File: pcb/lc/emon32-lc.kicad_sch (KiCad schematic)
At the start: 49 parts, among them J3 Conn_02x05_Odd_Even, J4 RJ12, J5 Conn_Coaxial, J6 USB_C_Receptacle_USB2.0, J7 Conn_01x03_Male, J8 Conn_02x04_Odd_Even, J9 Conn_01x03_Male, SW1 SW_Push, U2 AT24CS01-STUM, U3 ATSAMD11D14A-M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

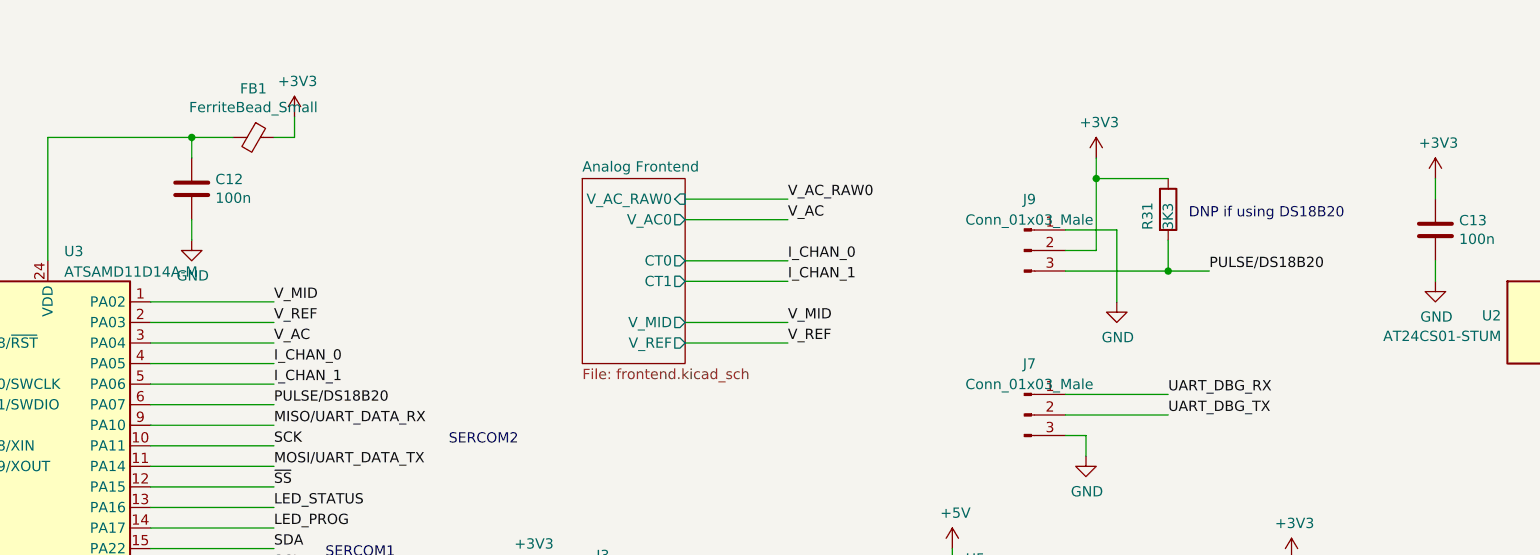
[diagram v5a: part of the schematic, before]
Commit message: * [LC]
  - Move ESP header out of RFM footprint to remove short risk
  - Remove all vias inside RFM footprint
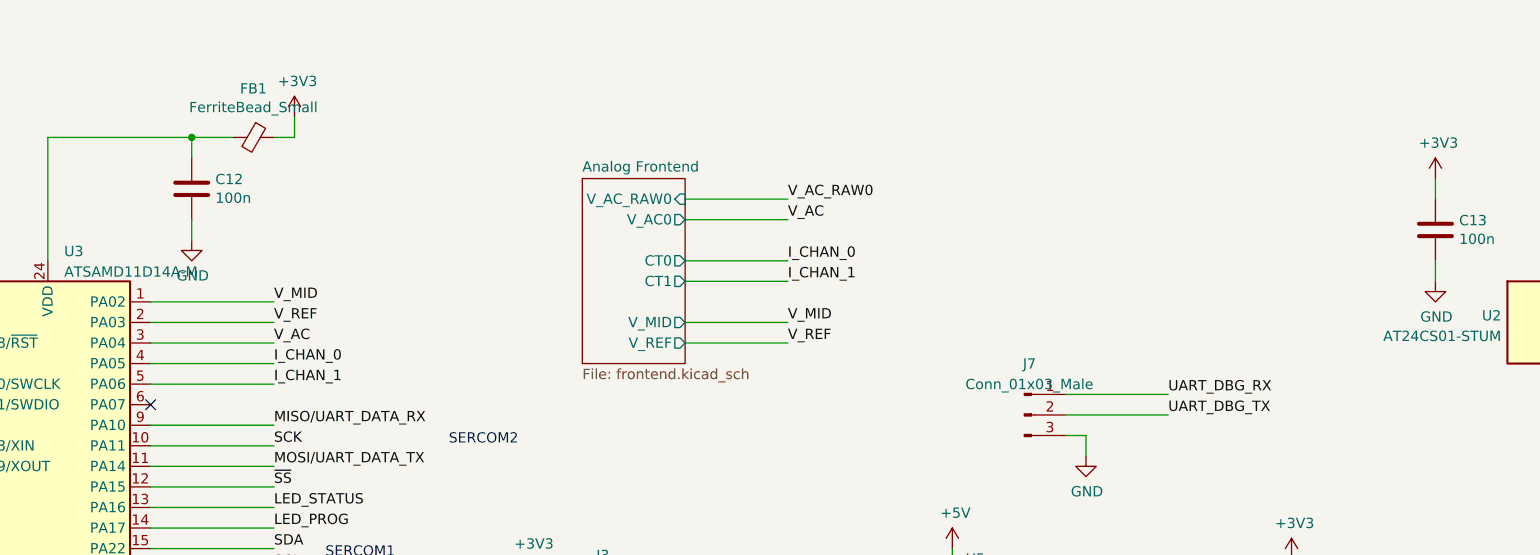
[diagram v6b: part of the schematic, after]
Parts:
- removed J9: Conn_01x03_Male, Connector_PinHeader_2.54mm:PinHeader_1x03_P2.54mm_Vertical, symbol Connector:Conn_01x03_Male
- removed R31: 3K3, Resistor_SMD:R_0402_1005Metric, symbol Device:R
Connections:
- net PULSE/DS18B20: no longer names the net of U3.6 (PA07)
- no-connect marks 18 -> 19
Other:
- note removed: "DNP if using DS18B20"
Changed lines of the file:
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@@
   (junction (at 27.94 24.13) (diameter 0) (color 0 0 0 0)
   )
-  (junction (at 177.8 25.4) (diameter 0) (color 0 0 0 0)
-  )
   (junction (at 124.46 129.54) (diameter 0) (color 0 0 0 0)
   )
   (junction (at 107.95 82.55) (diameter 0) (color 0 0 0 0)
-  )
-  (junction (at 186.69 36.83) (diameter 0) (color 0 0 0 0)
   )
   (junction (at 66.04 20.32) (diameter 0) (color 0 0 0 0)
@@
   (no_connect (at 60.96 81.28))
   (no_connect (at 50.8 157.48))
+  (no_connect (at 60.96 53.34))
   (no_connect (at 248.92 102.87))
   (wire (pts (xy 80.01 171.45) (xy 80.01 185.42))
@@
     (stroke (width 0) (type default))
   )
-  (wire (pts (xy 177.8 25.4) (xy 186.69 25.4))
-    (stroke (width 0) (type default))
-  )
   (wire (pts (xy 219.71 144.78) (xy 228.6 144.78))
     (stroke (width 0) (type default))
@@
     (stroke (width 0) (type default))
   )
-  (wire (pts (xy 177.8 25.4) (xy 177.8 22.86))
-    (stroke (width 0) (type default))
-  )
   (wire (pts (xy 96.52 129.54) (xy 100.33 129.54))
     (stroke (width 0) (type default))
@@
     (stroke (width 0) (type default))
   )
-  (wire (pts (xy 180.34 31.75) (xy 180.34 40.64))
-    (stroke (width 0) (type default))
-  )
   (wire (pts (xy 118.11 129.54) (xy 120.65 129.54))
     (stroke (width 0) (type default))
@@
     (stroke (width 0) (type default))
   )
-  (wire (pts (xy 186.69 33.02) (xy 186.69 36.83))
-    (stroke (width 0) (type default))
-  )
   (wire (pts (xy 60.96 43.18) (xy 76.2 43.18))
     (stroke (width 0) (type default))
@@
     (stroke (width 0) (type default))
   )
-  (wire (pts (xy 60.96 53.34) (xy 76.2 53.34))
-    (stroke (width 0) (type default))
-  )
   (wire (pts (xy 60.96 48.26) (xy 76.2 48.26))
     (stroke (width 0) (type default))
@@
     (stroke (width 0) (type default))
   )
-  (wire (pts (xy 173.99 34.29) (xy 177.8 34.29))
-    (stroke (width 0) (type default))
-  )
   (wire (pts (xy 241.3 142.24) (xy 247.65 142.24))
     (stroke (width 0) (type default))
@@
     (stroke (width 0) (type default))
   )
-  (wire (pts (xy 173.99 36.83) (xy 186.69 36.83))
-    (stroke (width 0) (type default))
-  )
   (wire (pts (xy 25.4 88.9) (xy 22.86 88.9))
     (stroke (width 0) (type default))
@@
     (stroke (width 0) (type default))
   )
-  (wire (pts (xy 177.8 25.4) (xy 177.8 34.29))
-    (stroke (width 0) (type default))
-  )
   (wire (pts (xy 50.8 129.54) (xy 69.85 129.54))
     (stroke (width 0) (type default))
@@
     (stroke (width 0) (type default))
   )
-  (wire (pts (xy 173.99 31.75) (xy 180.34 31.75))
-    (stroke (width 0) (type default))
-  )
   (wire (pts (xy 176.53 57.15) (xy 176.53 59.69))
     (stroke (width 0) (type default))
@@
     (stroke (width 0) (type default))
   )
-  (wire (pts (xy 186.69 36.83) (xy 191.77 36.83))
-    (stroke (width 0) (type default))
-  )
   (wire (pts (xy 27.94 50.8) (xy 25.4 50.8))
     (stroke (width 0) (type default))
@@
   (wire (pts (xy 139.7 152.4) (xy 139.7 149.86))
     (stroke (width 0) (type default))
-  )
-  (text "DNP if using DS18B20" (at 189.23 30.48 0)
-    (effects (font (size 1.27 1.27)) (justify left bottom))
   )
   (text "emon32 Low Cost" (at 177.8 171.45 0)
@@
     (effects (font (size 1.27 1.27)) (justify left bottom))
   )
-  (label "PULSE{slash}DS18B20" (at 191.77 36.83 0) (fields_autoplaced)
-    (effects (font (size 1.27 1.27)) (justify left bottom))
-  )
   (label "MOSI{slash}UART_DATA_TX" (at 219.71 144.78 180) (fields_autoplaced)
     (effects (font (size 1.27 1.27)) (justify right bottom))
@@
   )
   (label "V_AC" (at 76.2 45.72 0) (fields_autoplaced)
-    (effects (font (size 1.27 1.27)) (justify left bottom))
-  )
-  (label "PULSE{slash}DS18B20" (at 76.2 53.34 0) (fields_autoplaced)
     (effects (font (size 1.27 1.27)) (justify left bottom))
   )
@@
     )
   )
-  (symbol (lib_id "power:+3V3") (at 177.8 22.86 0) (unit 1)
-    (in_bom yes) (on_board yes) (dnp no)
-    (property "Reference" "#PWR0133" (at 177.8 26.67 0)
-      (effects (font (size 1.27 1.27)) hide)
-    )
-    (property "Value" "+3V3" (at 178.181 18.4658 0)
-      (effects (font (size 1.27 1.27)))
-    )
-    (property "Footprint" "" (at 177.8 22.86 0)
-      (effects (font (size 1.27 1.27)) hide)
-    )
-    (property "Datasheet" "" (at 177.8 22.86 0)
-      (effects (font (size 1.27 1.27)) hide)
-    )
-    (pin "1")
-    (instances
-      (project "emon32-lc"
-        (path "/1ce55b16-b0c6-4370-b9f7-e3a4b0029dbc"
-          (reference "#PWR0133") (unit 1)
-        )
-      )
-    )
-  )
   (symbol (lib_id "Memory_EEPROM:AT24CS01-STUM") (at 236.22 43.18 0) (unit 1)
     (in_bom yes) (on_board yes) (dnp no) (fields_autoplaced)
@@
         (path "/1ce55b16-b0c6-4370-b9f7-e3a4b0029dbc"
           (reference "R29") (unit 1)
-        )
-      )
-    )
-  )
-  (symbol (lib_id "Device:R") (at 186.69 29.21 0) (unit 1)
-    (in_bom yes) (on_board yes) (dnp no)
-    (property "Reference" "R31" (at 184.15 31.75 90)
-      (effects (font (size 1.27 1.27)) (justify left))
-    )
-    (property "Value" "3K3" (at 186.69 31.75 90)
-      (effects (font (size 1.27 1.27)) (justify left))
-    )
-    (property "Footprint" "Resistor_SMD:R_0402_1005Metric" (at 184.912 29.21 90)
-      (effects (font (size 1.27 1.27)) hide)
-    )
-    (property "Datasheet" "~" (at 186.69 29.21 0)
-      (effects (font (size 1.27 1.27)) hide)
-    )
-    (pin "1")
-    (pin "2")
-    (instances
-      (project "emon32-lc"
-        (path "/1ce55b16-b0c6-4370-b9f7-e3a4b0029dbc"
-          (reference "R31") (unit 1)
         )
       )
@@
     )
   )
-  (symbol (lib_id "Connector:Conn_01x03_Male") (at 168.91 34.29 0) (unit 1)
-    (in_bom yes) (on_board yes) (dnp no) (fields_autoplaced)
-    (property "Reference" "J9" (at 169.545 27.974 0)
-      (effects (font (size 1.27 1.27)))
-    )
-    (property "Value" "Conn_01x03_Male" (at 169.545 30.5109 0)
-      (effects (font (size 1.27 1.27)))
-    )
-    (property "Footprint" "Connector_PinHeader_2.54mm:PinHeader_1x03_P2.54mm_Vertical" (at 168.91 34.29 0)
-      (effects (font (size 1.27 1.27)) hide)
-    )
-    (property "Datasheet" "~" (at 168.91 34.29 0)
-      (effects (font (size 1.27 1.27)) hide)
-    )
-    (pin "1")
-    (pin "2")
-    (pin "3")
-    (instances
-      (project "emon32-lc"
-        (path "/1ce55b16-b0c6-4370-b9f7-e3a4b0029dbc"
-          (reference "J9") (unit 1)
-        )
-      )
-    )
-  )
   (symbol (lib_id "Connector:Conn_Coaxial") (at 259.08 91.44 0) (unit 1)
     (in_bom yes) (on_board yes) (dnp no) (fields_autoplaced)
@@
         )
       )
-    )
-  )
-  (symbol (lib_id "power:GND") (at 180.34 40.64 0) (unit 1)
-    (in_bom yes) (on_board yes) (dnp no)
-    (property "Reference" "#PWR0122" (at 180.34 46.99 0)
-      (effects (font (size 1.27 1.27)) hide)
-    )
-    (property "Value" "GND" (at 180.467 45.0342 0)
-      (effects (font (size 1.27 1.27)))
-    )
-    (property "Footprint" "" (at 180.34 40.64 0)
-      (effects (font (size 1.27 1.27)) hide)
-    )
-    (property "Datasheet" "" (at 180.34 40.64 0)
-      (effects (font (size 1.27 1.27)) hide)
-    )
-    (pin "1")
-    (instances
-      (project "emon32-lc"
-        (path "/1ce55b16-b0c6-4370-b9f7-e3a4b0029dbc"
-          (reference "#PWR0122") (unit 1)
-        )
-      )

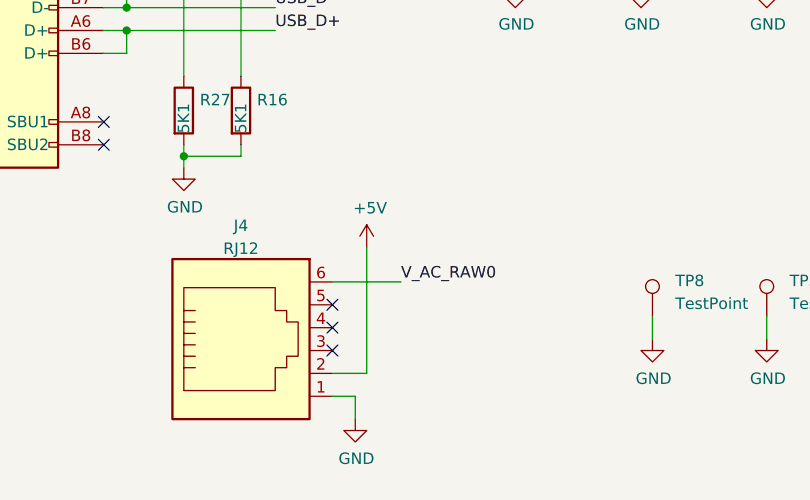
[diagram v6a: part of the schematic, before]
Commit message: * [LC]
  - Change to 8P8C header
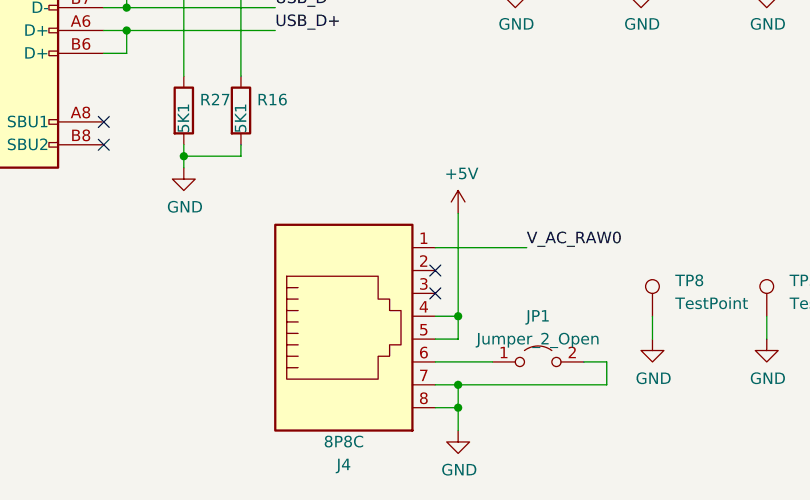
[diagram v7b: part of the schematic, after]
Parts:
- removed J4: RJ12, Connector_RJ:RJ12_Amphenol_54601, symbol Connector:RJ12
- added J4: 8P8C, Connector_RJ:RJ45_Amphenol_54602-x08_Horizontal, symbol Connector:8P8C
- added JP1: Jumper_2_Open, Jumper:SolderJumper-2_P1.3mm_Open_TrianglePad1.0x1.5mm, symbol Jumper:Jumper_2_Open
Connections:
- net +5V: now also J4.4, J4.5
- net GND: now also J4.7, J4.8, JP1.2 (B)
- net V_AC_RAW0: now also J4.1
- new net: J4.6, JP1.1 (A)
- no-connect marks 19 -> 18
